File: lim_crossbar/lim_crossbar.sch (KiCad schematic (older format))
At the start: 13 parts, among them J1 Conn_02x12_Counter_Clockwise, J2 Conn_02x12_Counter_Clockwise, J3 Conn_02x12_Counter_Clockwise, J4 Conn_02x08_Odd_Even, J5 Conn_02x08_Odd_Even

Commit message: otter crossbars shortened
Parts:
- J1, J2, J3: mfg (none) -> samtec; mfg_part (none) -> SQT-112-03-F-D
- J4, J5: mfg (none) -> samtec; mfg_part (none) -> MECF-08-01-L-DV-NP-WT
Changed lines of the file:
@@
 F 2 "custom:PinSocket_2x12_P2.00mm_Vertical_EDGE" H 7600 2300 50  0001 C CNN
 F 3 "~" H 7600 2300 50  0001 C CNN
+F 4 "samtec" H 7600 2300 50  0001 C CNN "mfg"
+F 5 "SQT-112-03-F-D" H 7600 2300 50  0001 C CNN "mfg_part"
 	1    7600 2300
 	0    1    1    0
@@
 F 2 "custom:PinSocket_2x12_P2.00mm_Vertical_EDGE" H 5600 2300 50  0001 C CNN
 F 3 "~" H 5600 2300 50  0001 C CNN
+F 4 "samtec" H 5600 2300 50  0001 C CNN "mfg"
+F 5 "SQT-112-03-F-D" H 5600 2300 50  0001 C CNN "mfg_part"
 	1    5600 2300
 	0    1    1    0
@@
 F 2 "custom:PinSocket_2x12_P2.00mm_Vertical_EDGE" H 3700 2300 50  0001 C CNN
 F 3 "~" H 3700 2300 50  0001 C CNN
+F 4 "samtec" V 3700 2300 50  0001 C CNN "mfg"
+F 5 "SQT-112-03-F-D" V 3700 2300 50  0001 C CNN "mfg_part"
 	1    3700 2300
 	0    1    1    0
@@
 F 2 "custom:Samtec_MECF-08-0_-NP-L-DV_2x08_P1.27mm_Edge_mod" H 8200 4800 50  0001 C CNN
 F 3 "~" H 8200 4800 50  0001 C CNN
+F 4 "samtec" H 8200 4800 50  0001 C CNN "mfg"
+F 5 "MECF-08-01-L-DV-NP-WT" H 8200 4800 50  0001 C CNN "mfg_part"
 	1    8200 4800
 	0    -1   -1   0
@@
 F 2 "custom:Samtec_MECF-08-0_-NP-L-DV_2x08_P1.27mm_Edge_mod" H 3200 4800 50  0001 C CNN
 F 3 "~" H 3200 4800 50  0001 C CNN
+F 4 "samtec" H 3200 4800 50  0001 C CNN "mfg"
+F 5 "MECF-08-01-L-DV-NP-WT" H 3200 4800 50  0001 C CNN "mfg_part"
 	1    3200 4800
 	0    -1   -1   0

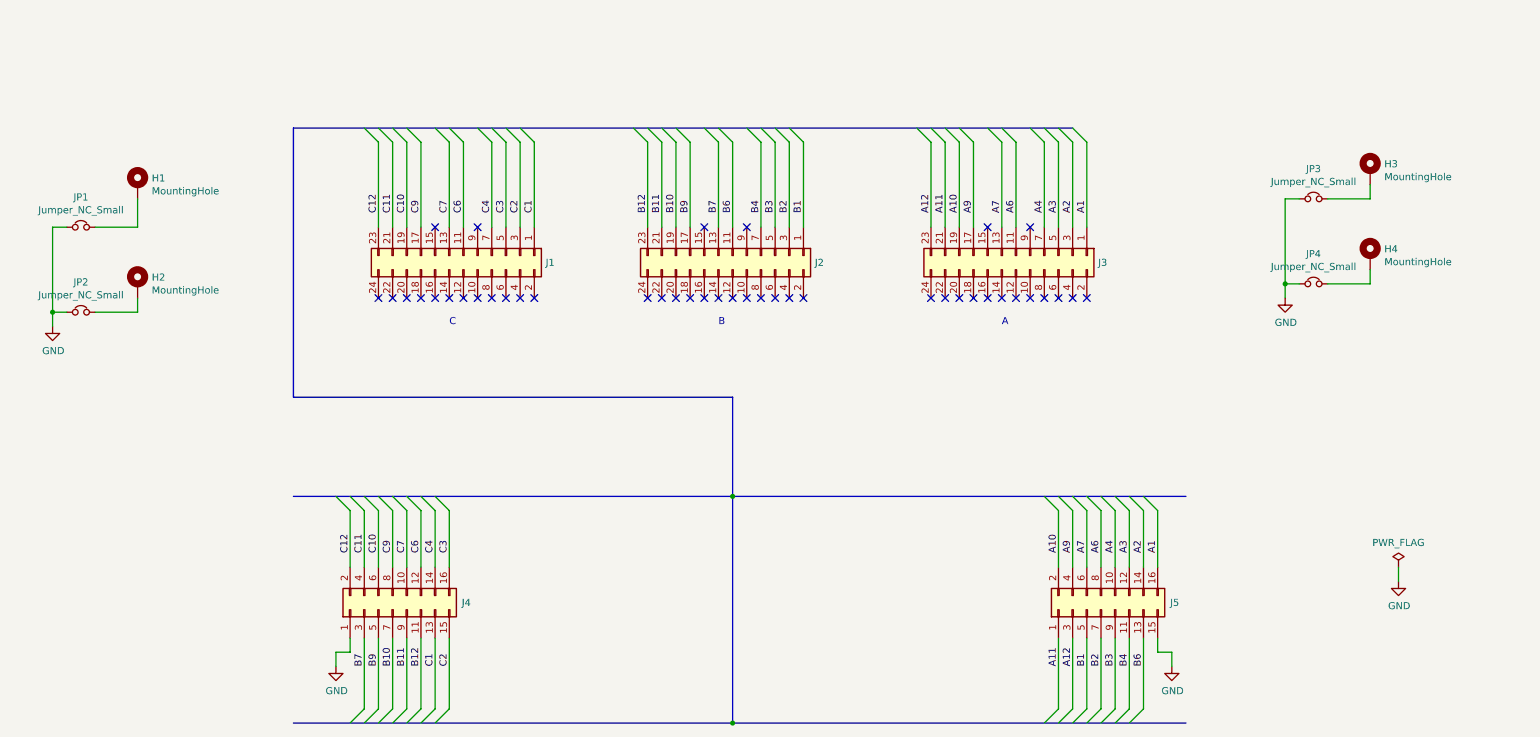
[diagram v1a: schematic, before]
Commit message: fix lim baseboard bug
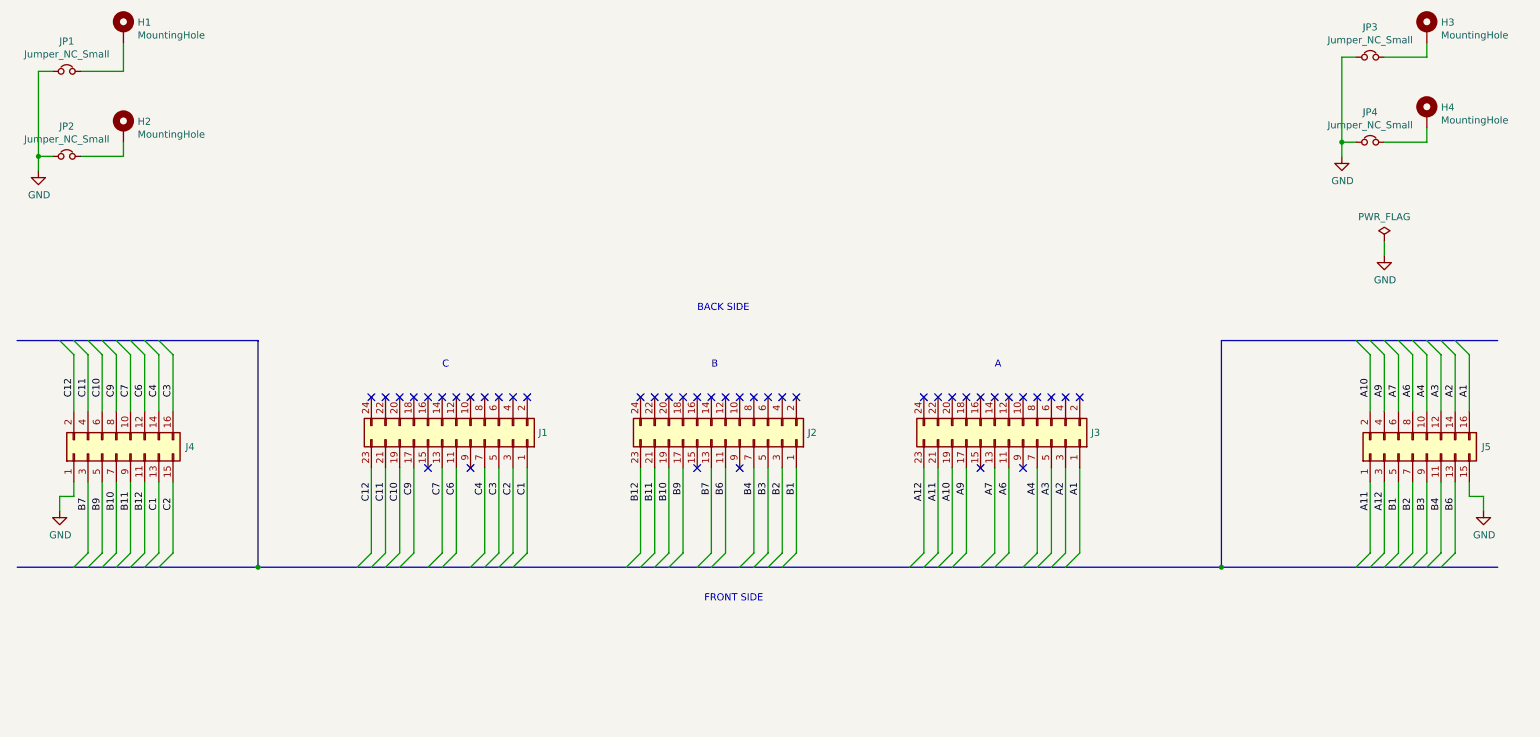
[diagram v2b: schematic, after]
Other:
- note added: "BACK SIDE"
- note added: "FRONT SIDE"
- moved on the sheet: H1, H2, H3, H4, J1, J2, J3, J4, J5, JP1, JP2, JP3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
